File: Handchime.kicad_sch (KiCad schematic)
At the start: 23 parts, among them J1 USB_C_Receptacle_USB2.0_16P, J2 Pins, J3 SWD, SW0 BOOT, SW1 Row 0, Col 0, SW2 Row 0, Col 1, U1 STM32C071GBUx, U2 PRTR5V0U2X, U3 XC6206P332MR-G

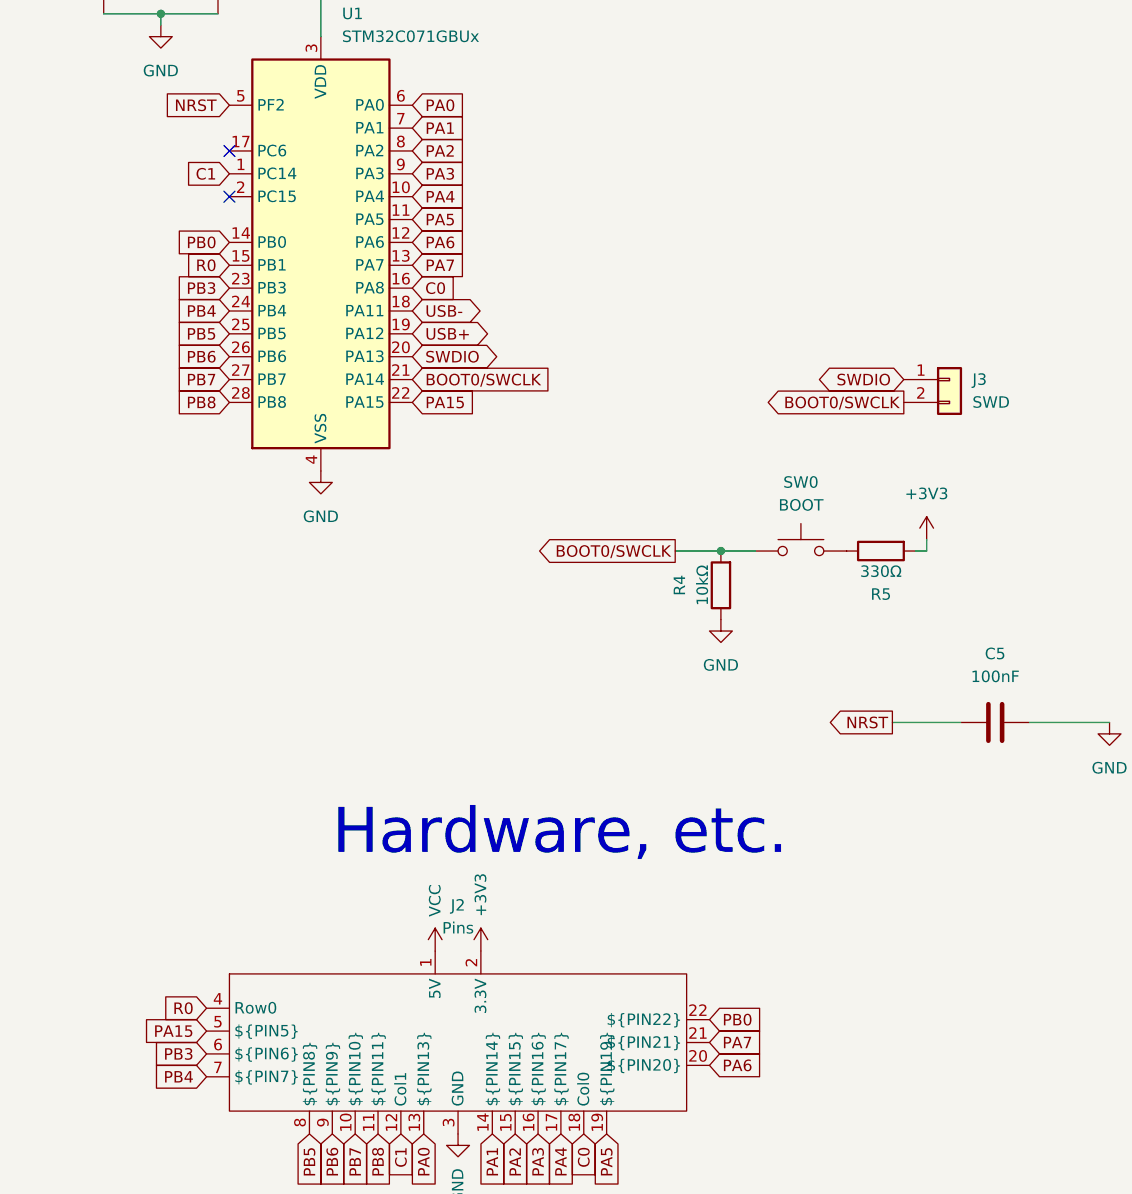
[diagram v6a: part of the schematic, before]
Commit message: Add RGB pull-up to edge pin 22
PB0 has the following timers available for driving RGB LEDs using PWM:

 * TIM3_CH3
 * TIM1_CH2N
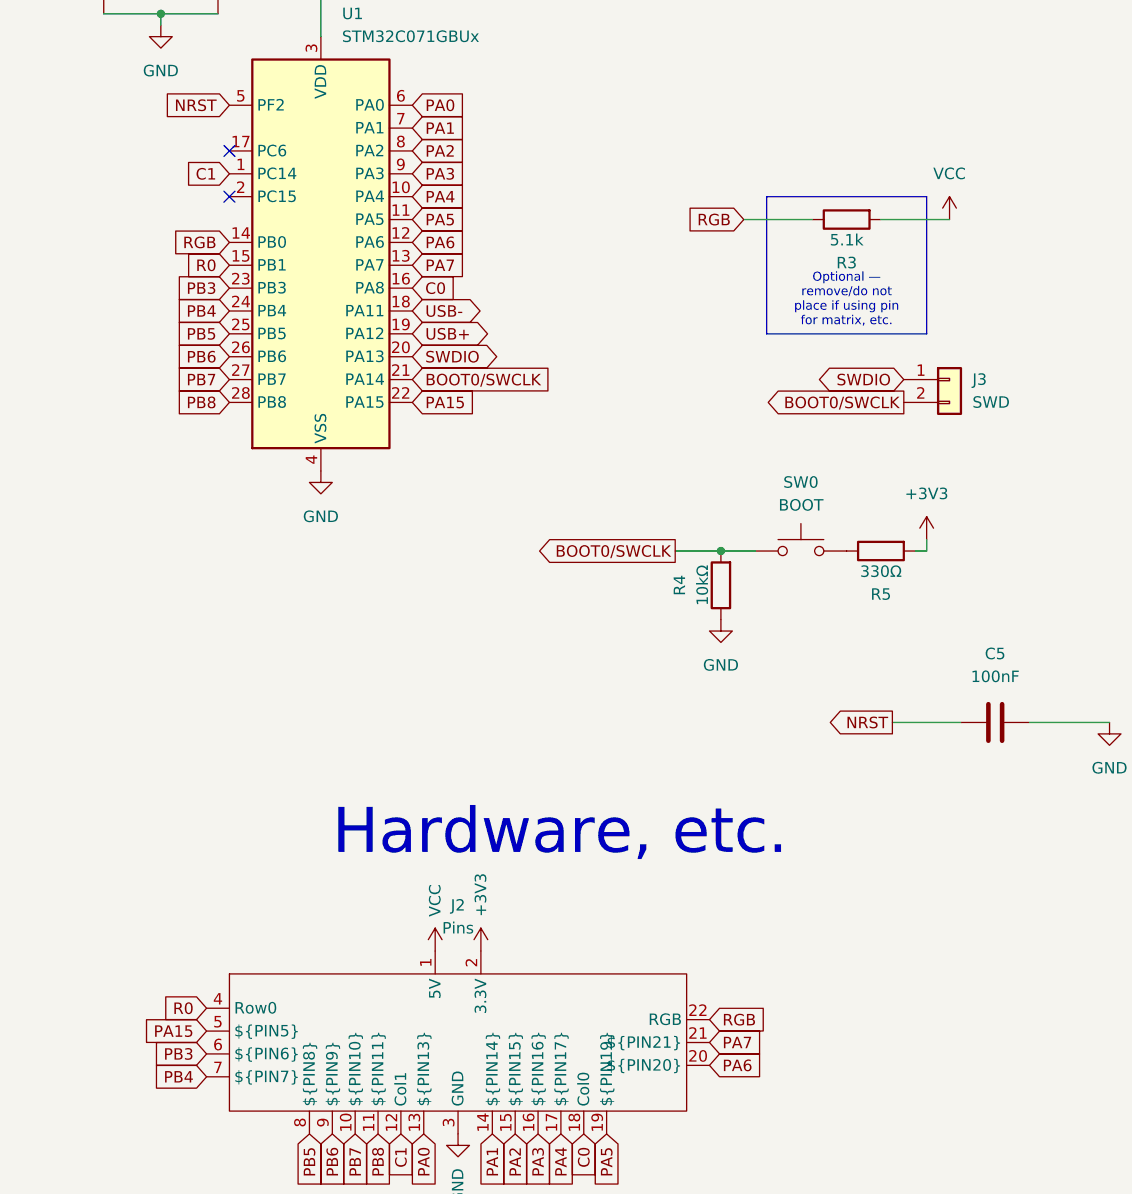
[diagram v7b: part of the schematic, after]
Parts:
- added R3: 5.1k, Resistor_SMD:R_0603_1608Metric, symbol Device:R
- J2: PIN22 A0 -> (none)
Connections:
- net VCC: now also R3.2
- net PB0 renamed RGB
- net RGB: now also R3.1
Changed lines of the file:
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@@
 		)
 	)
+	(text_box "Optional — remove/do not place if using pin for matrix, etc."
+		(exclude_from_sim no)
+		(at 238.76 45.72 0)
+		(size 17.78 15.24)
+		(margins 0.9525 0.9525 0.9525 0.9525)
+		(stroke
+			(width 0)
+			(type solid)
+		)
+		(fill
+			(type none)
+		)
+		(effects
+			(font
+				(size 1 1)
+			)
+			(justify bottom)
+		)
+	)
 	(junction
 		(at 138.43 149.86)
@@
 	(wire
 		(pts
+			(xy 259.08 48.26) (xy 251.46 48.26)
+		)
+		(stroke
+			(width 0)
+			(type default)
+		)
+	)
+	(wire
+		(pts
 			(xy 133.35 149.86) (xy 138.43 149.86)
 		)
@@
 	(wire
 		(pts
+			(xy 236.22 48.26) (xy 243.84 48.26)
+		)
+		(stroke
+			(width 0)
+			(type default)
+		)
+	)
+	(wire
+		(pts
 			(xy 125.73 158.75) (xy 125.73 157.48)
 		)
@@
 		)
 	)
-	(global_label "PB0"
+	(global_label "RGB"
 		(shape input)
 		(at 232.41 137.16 0)
@@
 		)
 		(property "Intersheetrefs" "${INTERSHEET_REFS}"
-			(at 238.3305 137.16 0)
+			(at 238.4645 137.16 0)
 			(hide yes)
 			(show_name no)
@@
 		)
 	)
+	(global_label "RGB"
+		(shape input)
+		(at 236.22 48.26 180)
+		(fields_autoplaced yes)
+		(effects
+			(font
+				(size 1.27 1.27)
+			)
+			(justify right)
+		)
+		(property "Intersheetrefs" "${INTERSHEET_REFS}"
+			(at 230.1655 48.26 0)
+			(hide yes)
+			(show_name no)
+			(do_not_autoplace no)
+			(effects
+				(font
+					(size 1.27 1.27)
+				)
+				(justify right)
+			)
+		)
+	)
 	(global_label "PB3"
 		(shape input)
@@
 		)
 	)
-	(global_label "PB0"
+	(global_label "PA5"
 		(shape input)
-		(at 179.07 50.8 180)
+		(at 220.98 149.86 270)
 		(fields_autoplaced yes)
 		(effects
@@
 		)
 		(property "Intersheetrefs" "${INTERSHEET_REFS}"
-			(at 173.1495 50.8 0)
+			(at 220.98 155.5087 90)
 			(hide yes)
 			(show_name no)
@@
 		)
 	)
-	(global_label "PA5"
+	(global_label "RGB"
 		(shape input)
-		(at 220.98 149.86 270)
+		(at 179.07 50.8 180)
 		(fields_autoplaced yes)
 		(effects
@@
 		)
 		(property "Intersheetrefs" "${INTERSHEET_REFS}"
-			(at 220.98 155.5087 90)
+			(at 173.0155 50.8 0)
 			(hide yes)
 			(show_name no)
@@
 	)
 	(symbol
+		(lib_id "power:VCC")
+		(at 259.08 48.26 0)
+		(unit 1)
+		(body_style 1)
+		(exclude_from_sim no)
+		(in_bom yes)
+		(on_board yes)
+		(in_pos_files yes)
+		(dnp no)
+		(fields_autoplaced yes)
+		(property "Reference" "#PWR04"
+			(at 259.08 52.07 0)
+			(hide yes)
+			(show_name no)
+			(do_not_autoplace no)
+			(effects
+				(font
+					(size 1.27 1.27)
+				)
+			)
+		)
+		(property "Value" "VCC"
+			(at 259.08 43.18 0)
+			(show_name no)
+			(do_not_autoplace no)
+			(effects
+				(font
+					(size 1.27 1.27)
+				)
+			)
+		)
+		(property "Footprint" ""
+			(at 259.08 48.26 0)
+			(hide yes)
+			(show_name no)
+			(do_not_autoplace no)
+			(effects
+				(font
+					(size 1.27 1.27)
+				)
+			)
+		)
+		(property "Datasheet" ""
+			(at 259.08 48.26 0)
+			(hide yes)
+			(show_name no)
+			(do_not_autoplace no)
+			(effects
+				(font
+					(size 1.27 1.27)
+				)
+			)
+		)
+		(property "Description" ""
+			(at 259.08 48.26 0)
+			(hide yes)
+			(show_name no)
+			(do_not_autoplace no)
+			(effects
+				(font
+					(size 1.27 1.27)
+				)
+			)
+		)
+		(pin "1"
+		)
+		(instances
+			(project "Handchime"
+				(path "/34400e51-cf83-464a-b3ec-e9a28a972a27"
+					(reference "#PWR04")
+					(unit 1)
+				)
+			)
+		)
+	)
+	(symbol
 		(lib_id "Device:C")
 		(at 177.8 21.59 0)
@@
 	)
 	(symbol
+		(lib_id "Device:R")
+		(at 247.65 48.26 90)
+		(mirror x)
+		(unit 1)
+		(body_style 1)
+		(exclude_from_sim no)
+		(in_bom yes)
+		(on_board yes)
+		(in_pos_files yes)
+		(dnp no)
+		(property "Reference" "R3"
+			(at 247.65 53.086 90)
+			(show_name no)
+			(do_not_autoplace no)
+			(effects
+				(font
+					(size 1.27 1.27)
+				)
+			)
+		)
+		(property "Value" "5.1k"
+			(at 247.65 50.546 90)
+			(show_name no)
+			(do_not_autoplace no)
+			(effects
+				(font
+					(size 1.27 1.27)
+				)
+			)
+		)
+		(property "Footprint" "Resistor_SMD:R_0603_1608Metric"
+			(at 247.65 46.482 90)
+			(hide yes)
+			(show_name no)
+			(do_not_autoplace no)
+			(effects
+				(font
+					(size 1.27 1.27)
+				)
+			)
+		)
+		(property "Datasheet" ""
+			(at 247.65 48.26 0)
+			(hide yes)
+			(show_name no)
+			(do_not_autoplace no)
+			(effects
+				(font
+					(size 1.27 1.27)
+				)
+			)
+		)
+		(property "Description" ""
+			(at 247.65 48.26 0)
+			(hide yes)
+			(show_name no)
+			(do_not_autoplace no)
+			(effects
+				(font
+					(size 1.27 1.27)
+				)
+			)
+		)
+		(property "LCSC" "C23186"
+			(at 247.65 48.26 90)
+			(hide yes)
+			(show_name no)
+			(do_not_autoplace no)
+			(effects
+				(font
+					(size 1.27 1.27)
+				)
+			)
+		)
+		(property "DigiKey" "311-5.10KHR"
+			(at 247.65 48.26 90)
+			(hide yes)
+			(show_name no)
+			(do_not_autoplace no)
+			(effects
+				(font
+					(size 1.27 1.27)
+				)
+			)
+		)
+		(pin "1"
+		)
+		(pin "2"
+		)
+		(instances
+			(project "Handchime"
+				(path "/34400e51-cf83-464a-b3ec-e9a28a972a27"
+					(reference "R3")
+					(unit 1)
+				)
+			)
+		)
+	)
+	(symbol
 		(lib_id "Switch:SW_Push")
 		(at 34.29 134.62 0)
@@
 			(at 204.47 139.7 0)
 			(hide yes)
-			(show_name no)
-			(do_not_autoplace no)
-			(effects
-				(font
-					(size 1.27 1.27)
-				)
-			)
-		)
-		(property "PIN22" "A0"
-			(at 204.47 139.7 0)
-			(hide yes)

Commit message: Clean-up silkscreens, tweak routing
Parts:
- J2: PIN10 B8 -> PB7; PIN11 A1 -> PB8; PIN13 A2 -> PA0; PIN14 A3 -> PA1; PIN15 A4 -> PA2; PIN16 A5 -> PA3; PIN17 A6 -> PA4; PIN19 A7 -> PA5; PIN20 B0 -> PA6; PIN21 B1 -> PA7; PIN5 B3 -> PA15; PIN6 B4 -> PB3; PIN7 B5 -> PB4; PIN8 B6 -> PB5; PIN9 B7 -> PB6
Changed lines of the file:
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@@
 			)
 		)
-		(property "PIN5" "B3"
+		(property "PIN5" "PA15"
 			(at 204.47 139.7 0)
 			(hide yes)
@@
 			)
 		)
-		(property "PIN6" "B4"
+		(property "PIN6" "PB3"
 			(at 204.47 139.7 0)
 			(hide yes)
@@
 			)
 		)
-		(property "PIN7" "B5"
+		(property "PIN7" "PB4"
 			(at 204.47 139.7 0)
 			(hide yes)
@@
 			)
 		)
-		(property "PIN8" "B6"
+		(property "PIN8" "PB5"
 			(at 204.47 139.7 0)
 			(hide yes)
@@
 			)
 		)
-		(property "PIN9" "B7"
+		(property "PIN9" "PB6"
 			(at 204.47 139.7 0)
 			(hide yes)
@@
 			)
 		)
-		(property "PIN10" "B8"
+		(property "PIN10" "PB7"
 			(at 204.47 139.7 0)
 			(hide yes)
@@
 			)
 		)
-		(property "PIN11" "A1"
+		(property "PIN11" "PB8"
 			(at 204.47 139.7 0)
 			(hide yes)
@@
 			)
 		)
-		(property "PIN13" "A2"
+		(property "PIN13" "PA0"
 			(at 204.47 139.7 0)
 			(hide yes)
@@
 			)
 		)
-		(property "PIN14" "A3"
+		(property "PIN14" "PA1"
 			(at 204.47 139.7 0)
 			(hide yes)
@@
 			)
 		)
-		(property "PIN15" "A4"
+		(property "PIN15" "PA2"
 			(at 204.47 139.7 0)
 			(hide yes)
@@
 			)
 		)
-		(property "PIN16" "A5"
+		(property "PIN16" "PA3"
 			(at 204.47 139.7 0)
 			(hide yes)
@@
 			)
 		)
-		(property "PIN17" "A6"
+		(property "PIN17" "PA4"
 			(at 204.47 139.7 0)
 			(hide yes)
@@
 			)
 		)
-		(property "PIN19" "A7"
+		(property "PIN19" "PA5"
 			(at 204.47 139.7 0)
 			(hide yes)
@@
 			)
 		)
-		(property "PIN20" "B0"
+		(property "PIN20" "PA6"
 			(at 204.47 139.7 0)
 			(hide yes)
@@
 			)
 		)
-		(property "PIN21" "B1"
+		(property "PIN21" "PA7"
 			(at 204.47 139.7 0)
 			(hide yes)
